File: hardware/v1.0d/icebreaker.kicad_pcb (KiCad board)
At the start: 4 copper layers, 73 x 37 mm, 191 parts, among them J1 Jumper, J10 Jumper, J11 Jumper, J12 Jumper, J13 Jumper, J14 Jumper, J15 Jumper, J16 Jumper, J17 Jumper, J18 Jumper, J19 Jumper, J2 Jumper, J20 Flash, J21 PMOD, J22 PMOD, J23 PMOD, J24 PMOD, J25 RGB Led, J26 5V AUX, J27 5V AUX, J28 CRESET, J29 Jumper, J3 Jumper, J30 Jumper, J31 RGB Led, J32 WS2812, J33 RGB Led, J34 SADD, J4 Jumper, J5 Jumper, J6 Jumper, J7 Jumper, J8 Jumper, J9 Jumper, P1 pkl_USB_OTG, P2 UP, P3 UP, P4 UP, P5 UP, P6 RAM_CS, Q1 BSS138, SW1 TACT, SW2 TACT, SW3 TACT, SW4 TACT, U1 93C46B-SOT-23-6, U2 3.3V, U3 1V2, U4 FT2232H, U5 W25Q, U6 ICE5LP4K-SG48, U7 12MHz

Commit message: Added more legend silkscreen to ears.
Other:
- board text added: "D 1"
- board text added: "D1"
- board text added: "D2"
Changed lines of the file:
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@@
   (general
     (thickness 1.6)
-    (drawings 401)
+    (drawings 440)
     (tracks 1560)
     (zones 0)
@@
     )
   )
-  (gr_text I2C (at 88.6 62.74 270) (layer B.SilkS)
-    (effects (font (size 1.5 1.5) (thickness 0.3)) (justify mirror))
+  (gr_text D1 (at 91.7 31 270) (layer F.SilkS)
+    (effects (font (size 0.75 0.75) (thickness 0.1875)))
+  )
+  (gr_text 3v3 (at 102.3 31 270) (layer F.SilkS)
+    (effects (font (size 0.75 0.75) (thickness 0.1875)))
+  )
+  (gr_text 5v0 (at 102.3 33.5 270) (layer F.SilkS)
+    (effects (font (size 0.75 0.75) (thickness 0.1875)))
+  )
+  (gr_circle (center 98.957 30.05) (end 98.957 30.05) (layer F.SilkS) (width 0.2))
+  (gr_line (start 99.338 29.796) (end 99.338 30.303999) (layer F.SilkS) (width 0.2))
+  (gr_line (start 99.719 30.05) (end 99.973 30.05) (layer F.SilkS) (width 0.2))
+  (gr_line (start 99.719 29.542) (end 99.719 30.558) (layer F.SilkS) (width 0.2))
+  (gr_line (start 99.719 34.45) (end 99.973 34.45) (layer F.SilkS) (width 0.2))
+  (gr_line (start 99.338 34.196) (end 99.338 34.703999) (layer F.SilkS) (width 0.2))
+  (gr_line (start 99.719 33.942) (end 99.719 34.958) (layer F.SilkS) (width 0.2))
+  (gr_circle (center 98.957 34.45) (end 98.957 34.45) (layer F.SilkS) (width 0.2))
+  (gr_text "D  1" (at 85.6 33.5 270) (layer B.SilkS)
+    (effects (font (size 0.7 0.7) (thickness 0.175)) (justify mirror))
+  )
+  (gr_line (start 91.3 33.999999) (end 91.3 33.000001) (layer B.SilkS) (width 0.2))
+  (gr_circle (center 90.500001 33.5) (end 90.500001 33.5) (layer B.SilkS) (width 0.2))
+  (gr_line (start 90.9 33.8) (end 90.9 33.2) (layer B.SilkS) (width 0.2))
+  (gr_line (start 91.3 33.500001) (end 91.6 33.5) (layer B.SilkS) (width 0.2))
+  (gr_text 5v0 (at 82.8 33.5 270) (layer B.SilkS)
+    (effects (font (size 0.75 0.75) (thickness 0.1875)) (justify mirror))
+  )
+  (gr_text D2 (at 91.6 64 270) (layer F.SilkS)
+    (effects (font (size 0.75 0.75) (thickness 0.1875)))
+  )
+  (gr_text D1 (at 91.7 61.5 270) (layer F.SilkS)
+    (effects (font (size 0.75 0.75) (thickness 0.1875)))
+  )
+  (gr_line (start 99.619 65.05) (end 99.873 65.05) (layer F.SilkS) (width 0.2))
+  (gr_line (start 99.619 64.542) (end 99.619 65.558) (layer F.SilkS) (width 0.2))
+  (gr_line (start 99.238 64.796) (end 99.238 65.303999) (layer F.SilkS) (width 0.2))
+  (gr_circle (center 98.857 65.05) (end 98.857 65.05) (layer F.SilkS) (width 0.2))
+  (gr_line (start 99.338 60.196) (end 99.338 60.703999) (layer F.SilkS) (width 0.2))
+  (gr_line (start 99.719 60.45) (end 99.973 60.45) (layer F.SilkS) (width 0.2))
+  (gr_circle (center 98.957 60.45) (end 98.957 60.45) (layer F.SilkS) (width 0.2))
+  (gr_line (start 99.719 59.942) (end 99.719 60.958) (layer F.SilkS) (width 0.2))
+  (gr_text 3v3 (at 102.3 61.5 270) (layer F.SilkS)
+    (effects (font (size 0.75 0.75) (thickness 0.1875)))
+  )
+  (gr_line (start 86.9 60.3) (end 86.9 60.5) (layer B.SilkS) (width 0.15))
+  (gr_line (start 86.9 65.2) (end 86.9 65) (layer B.SilkS) (width 0.15))
+  (gr_line (start 87.9 65.2) (end 86.9 65.2) (layer B.SilkS) (width 0.15))
+  (gr_line (start 87.6 60.307392) (end 86.9 60.307392) (layer B.SilkS) (width 0.15))
+  (gr_text D2 (at 88.4 65.1 270) (layer B.SilkS)
+    (effects (font (size 0.75 0.75) (thickness 0.1875)) (justify mirror))
+  )
+  (gr_text D1 (at 82.8 64 270) (layer B.SilkS)
+    (effects (font (size 0.75 0.75) (thickness 0.1875)) (justify mirror))
+  )
+  (gr_text 3v3 (at 82.8 61.5 270) (layer B.SilkS)
+    (effects (font (size 0.75 0.75) (thickness 0.1875)) (justify mirror))
+  )
+  (gr_line (start 88.3 60.8) (end 88.3 60.2) (layer B.SilkS) (width 0.2))
+  (gr_line (start 88.7 60.500001) (end 89 60.5) (layer B.SilkS) (width 0.2))
+  (gr_circle (center 87.900001 60.5) (end 87.900001 60.5) (layer B.SilkS) (width 0.2))
+  (gr_line (start 88.7 60.999999) (end 88.7 60.000001) (layer B.SilkS) (width 0.2))
+  (gr_text I2C (at 89.1 62.74 270) (layer B.SilkS)
+    (effects (font (size 1 1) (thickness 0.25)) (justify mirror))
   )
   (dimension 21 (width 0.3) (layer Dwgs.User)

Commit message: A bunch of DRC fixes and improvements.
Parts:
- moved R22 0.28 mm to (66.8, 52.8)
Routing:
- net /iCE_SS_B: track 33.7 -> 34.2 mm
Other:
- net class Default: clearance 0.149 -> 0.15
- rule trace_clearance: 0.149 -> 0.15
- rule trace_min: 0.149 -> 0.15

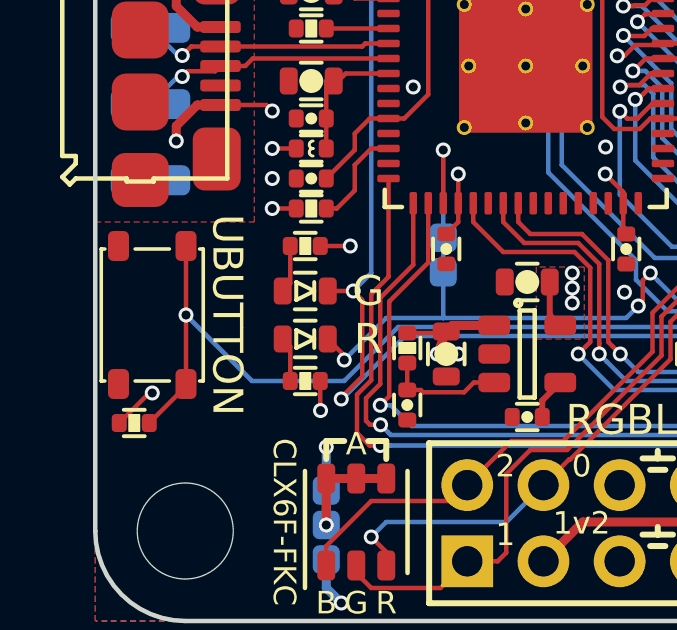
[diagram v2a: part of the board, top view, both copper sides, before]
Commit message: Some minor silkscreen label cleaning.
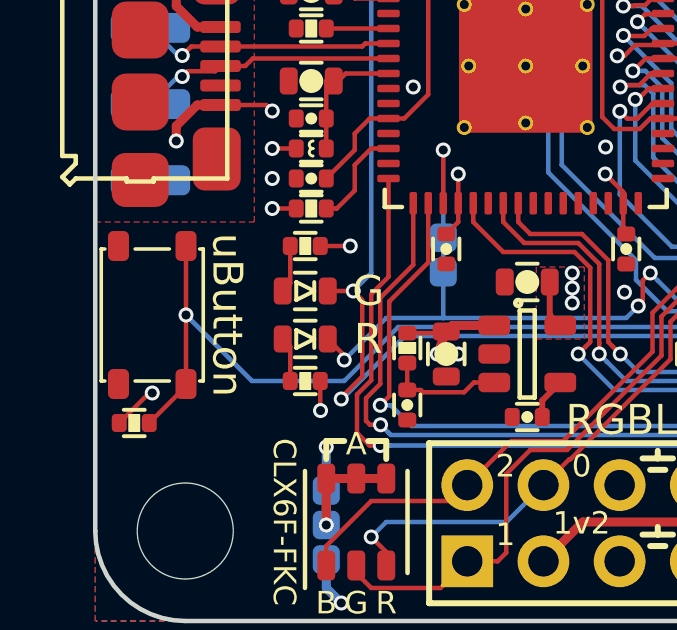
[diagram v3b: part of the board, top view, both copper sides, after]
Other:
- board text added: "3v3 5v0"
- board text added: "RGB0 1v2"
- board text added: "uButton"
- board text removed: "3v3 5v"
- board text removed: "5V"
- board text removed: "RGB0 1V2"
- board text removed: "UBUTTON"
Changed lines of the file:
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@@
     (effects (font (size 1 0.75) (thickness 0.1875)) (justify mirror))
   )
-  (gr_text 5V (at 34.25 43.75) (layer B.SilkS)
+  (gr_text +5V (at 34.4 43.75) (layer B.SilkS)
     (effects (font (size 1 0.75) (thickness 0.1875)) (justify mirror))
   )
@@
     (effects (font (size 1 0.6) (thickness 0.15)) (justify mirror))
   )
-  (gr_text "RGB0\n1V2" (at 44.95 58.8) (layer B.SilkS)
+  (gr_text "RGB0\n1v2" (at 44.95 58.8) (layer B.SilkS)
     (effects (font (size 1 0.6) (thickness 0.15)) (justify mirror))
   )
-  (gr_text "3v3\n5v" (at 50.1 58.8) (layer B.SilkS)
+  (gr_text "3v3\n5v0" (at 50.1 58.8) (layer B.SilkS)
     (effects (font (size 1 0.6) (thickness 0.15)) (justify mirror))
   )
@@
     (effects (font (size 0.75 0.75) (thickness 0.1875)))
   )
-  (gr_text UBUTTON (at 34.4 55.8 270) (layer F.SilkS)
+  (gr_text uButton (at 34.4 55.8 270) (layer F.SilkS)
     (effects (font (size 1 1) (thickness 0.25)))
   )
